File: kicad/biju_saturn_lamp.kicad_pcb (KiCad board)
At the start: 2 copper layers, 82.3 x 59.9 mm, 25 parts, among them J1 Barrel_Jack, J2 Conn_01x06, J3 Conn_01x02, J4 Conn_01x02, J5 Conn_01x02, SW1 SW_Push, U1 Pico, U2 74HC595, U3 PAM8302AAD

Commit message: update pcb
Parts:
- C4, C5: value 220uF -> 220nF
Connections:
- U2 pad 10: unconnected-(U2-~{SRCLR}-Pad10) -> VCC
- U2 pad 13: unconnected-(U2-~{OE}-Pad13) -> GND
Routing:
- net GND: track 45.4 -> 269.8 mm
- net VCC: track 153.5 -> 218.0 mm

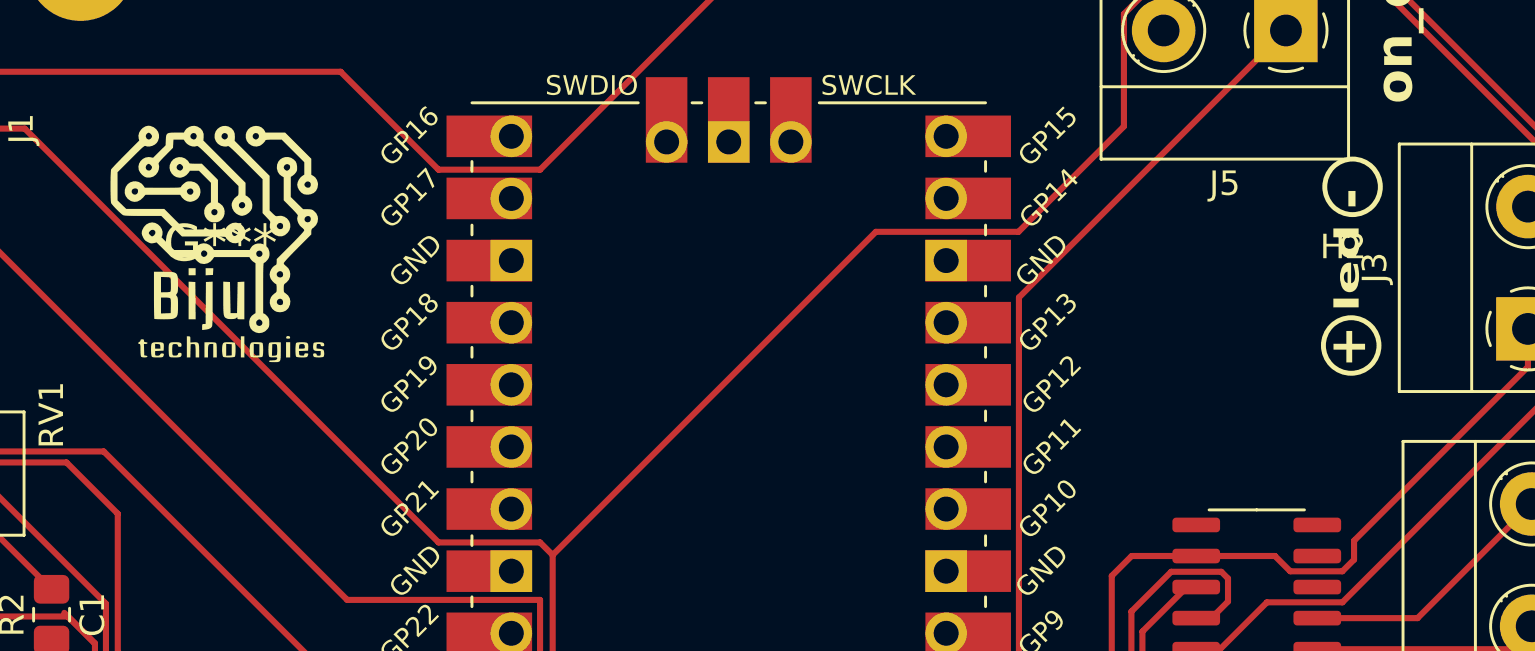
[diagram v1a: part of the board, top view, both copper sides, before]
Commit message: add logo to pcb
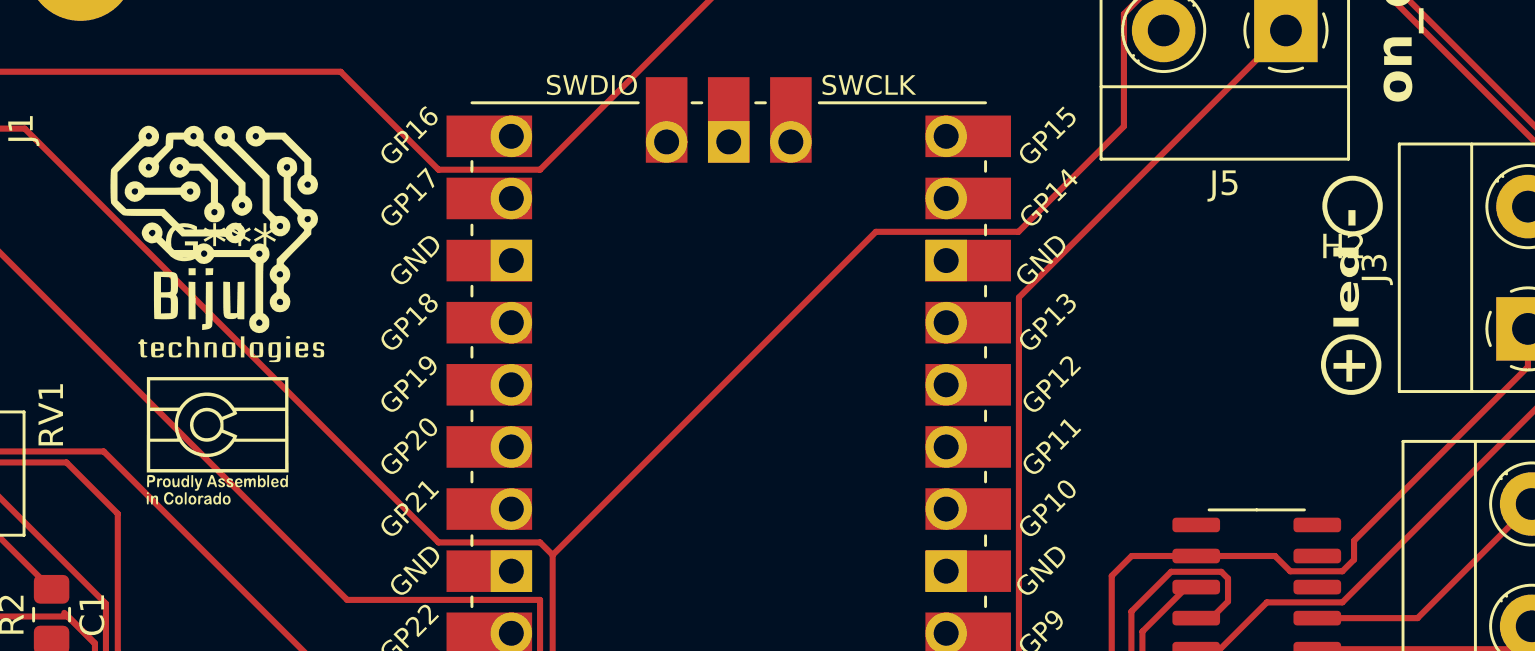
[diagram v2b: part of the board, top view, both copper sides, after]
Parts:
- added G***: LOGO, LOGO, F.Cu at (170.1, 113.5)

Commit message: update pcb
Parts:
- moved G*** 52.8 mm to (218.4, 125.7)
- moved G*** 52.8 mm to (211.6, 146.2)
- moved H3 9.14 mm to (180.3, 81.8)
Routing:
- net GND: track 269.8 -> 313.3 mm
- net VCC: track 218.0 -> 246.2 mm
- net GPIO8: track 53.5 -> 59.5 mm
- net 3v3_EN: track 119.0 -> 121.0 mm

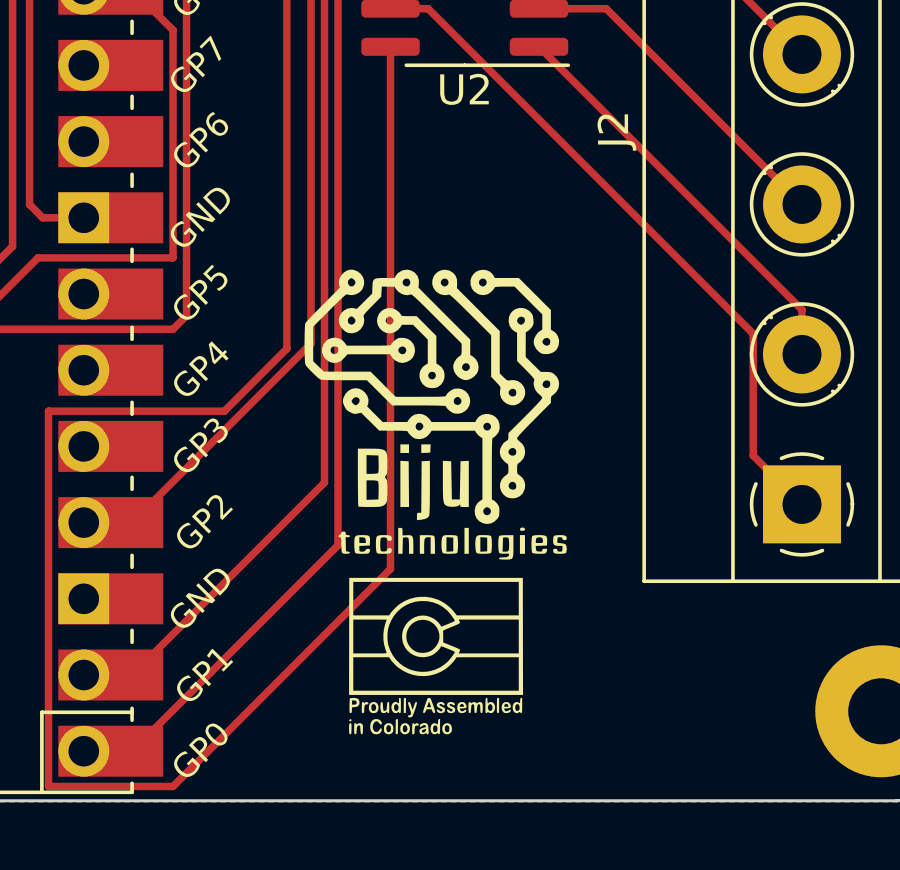
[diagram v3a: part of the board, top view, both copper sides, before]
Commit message: add logo to pcb
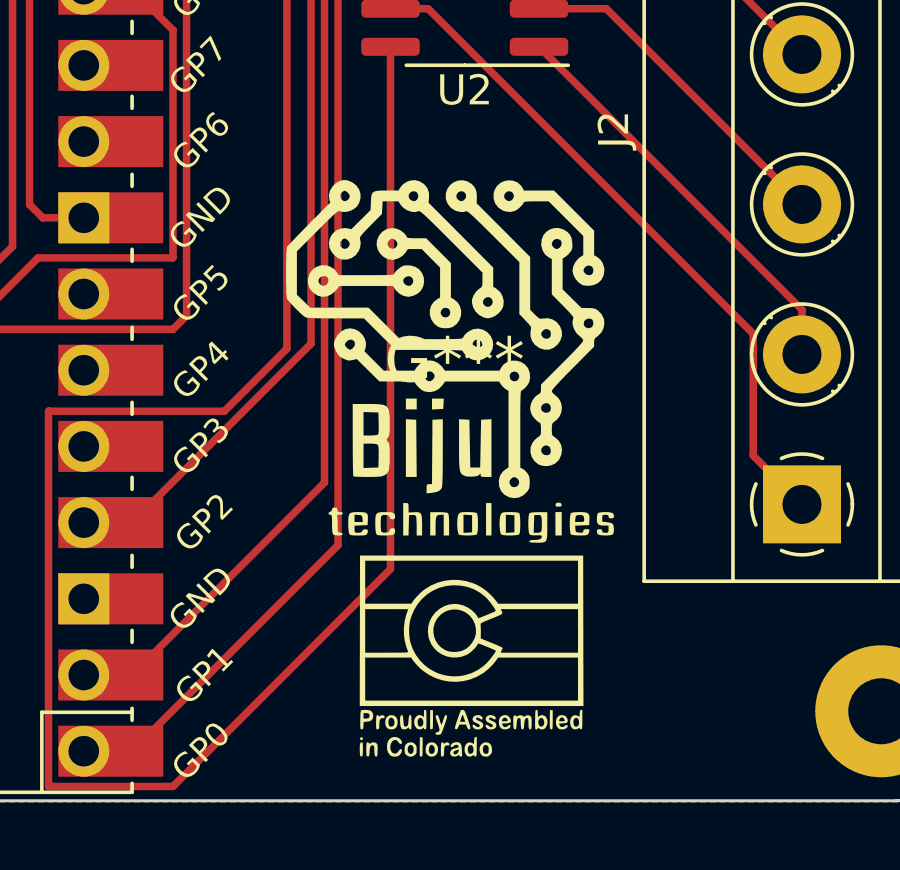
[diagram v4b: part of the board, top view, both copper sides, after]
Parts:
- removed the G*** at (211.6, 146.2)
- removed the G*** at (218.4, 125.7)
- added G***: LOGO, LOGO, F.Cu at (210.8, 149.7)
- added G***: LOGO, LOGO, F.Cu at (218.9, 124.0)

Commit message: update pcb
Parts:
- moved RV1 1.03 mm to (166.4, 99.1)
- moved R1 0.99 mm to (170.0, 112.3), turned to -90 degrees
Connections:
- U1 pad 18: unconnected-(U1-GND-Pad18) -> GND
- U1 pad 23: unconnected-(U1-GND-Pad23) -> GND
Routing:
- net GND: track 313.3 -> 229.3 mm
- net 3v3: track 70.5 -> 66.2 mm
- net Net-(C1-Pad2): track 2.54 -> 4.88 mm
- net Net-(C1-Pad1): track 7.53 -> 8.54 mm
- net Net-(U3-IN+): track 4.74 -> 3.86 mm
- net Net-(U3-~{SD}): track 26.5 -> 27.2 mm

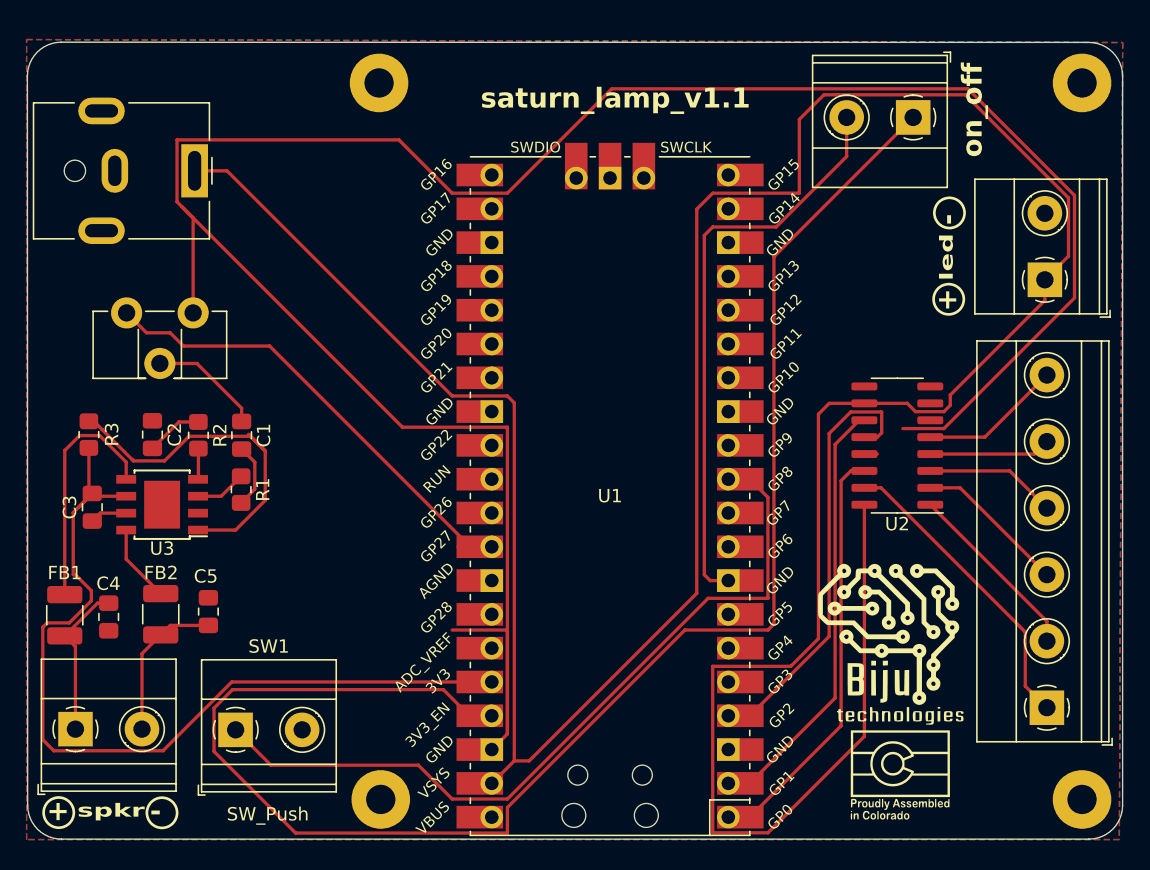
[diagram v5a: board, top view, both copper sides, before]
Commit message: fix on-off switch
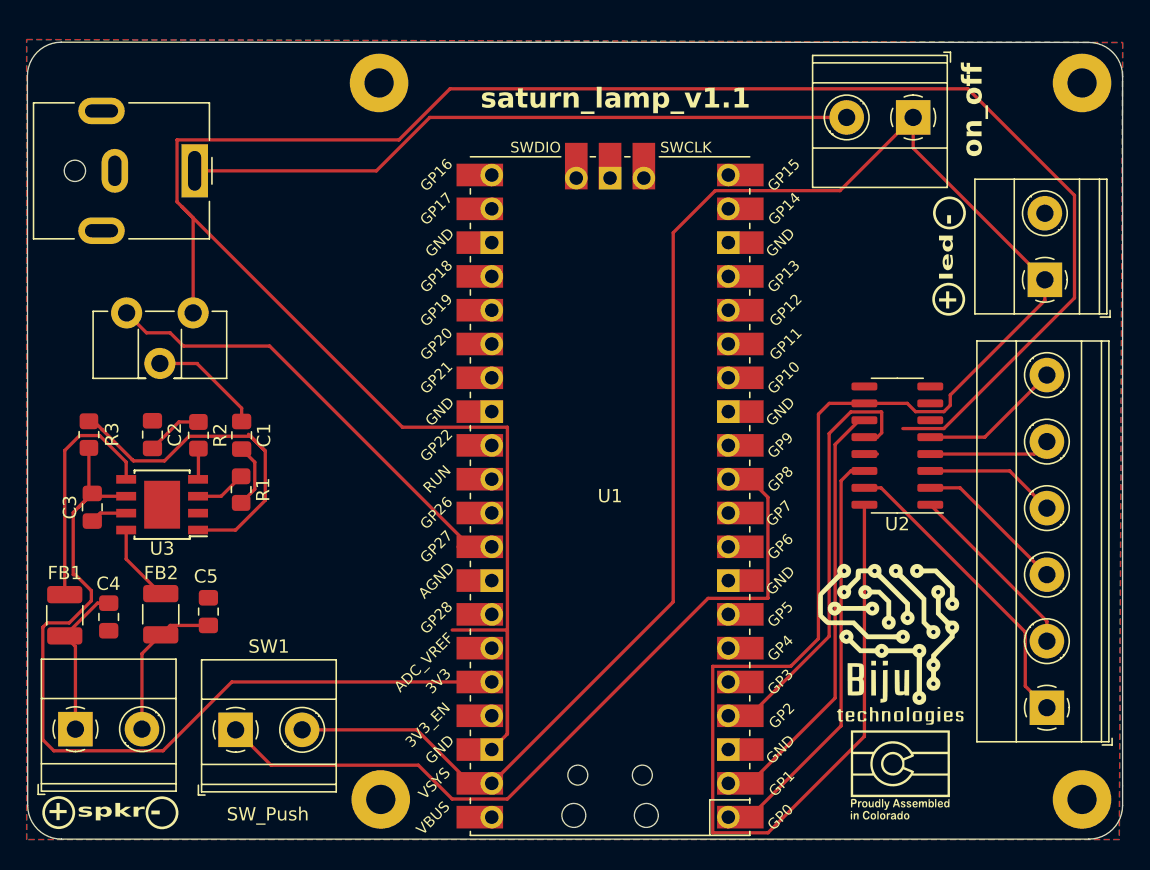
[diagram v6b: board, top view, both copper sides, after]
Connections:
- J1 pad 1: VCC -> Net-(J5-Pin_2)
- J5 pad 1: 3v3_EN -> VCC
- J5 pad 2: GND -> Net-(J5-Pin_2)
- SW1 pad 2: GND -> VCC
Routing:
- net 3v3_EN: track 121.0 -> 2.48 mm
- net VCC: track 246.7 -> 194.3 mm
- net Net-(J5-Pin_2): track 0.00 -> 50.7 mm
- net GND: track 229.3 -> 182.4 mm

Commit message: add base stl
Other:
- board text added: "JLCJLCJLCJLC"
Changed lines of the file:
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@@
     (fp_line (start 1.6 1.245) (end -1.6 1.245)
       (stroke (width 0.1) (type solid)) (layer "F.Fab"))
-    (pad "1" smd roundrect (at -1.55 0 270) (size 1.3 2.65) (layers "F.Cu" "F.Paste" "F.Mask") (roundrect_rratio 0.192308)
+    (pad "1" smd roundrect (at -1.55 0 270) (size 1.3 2.65) (layers "F.Cu" "F.Paste" "F.Mask") (roundrect_rratio 0.1923076923)
       (net 31 "Net-(U3-OUT+)") (pintype "passive"))
-    (pad "2" smd roundrect (at 1.55 0 270) (size 1.3 2.65) (layers "F.Cu" "F.Paste" "F.Mask") (roundrect_rratio 0.192308)
+    (pad "2" smd roundrect (at 1.55 0 270) (size 1.3 2.65) (layers "F.Cu" "F.Paste" "F.Mask") (roundrect_rratio 0.1923076923)
       (net 18 "Net-(J4-Pin_1)") (pintype "passive"))
     (model "${KICAD6_3DMODEL_DIR}/Resistor_SMD.3dshapes/R_1210_3225Metric.wrl"
@@
     (fp_line (start 1.6 1.245) (end -1.6 1.245)
       (stroke (width 0.1) (type solid)) (layer "F.Fab"))
-    (pad "1" smd roundrect (at -1.55 0 270) (size 1.3 2.65) (layers "F.Cu" "F.Paste" "F.Mask") (roundrect_rratio 0.192308)
+    (pad "1" smd roundrect (at -1.55 0 270) (size 1.3 2.65) (layers "F.Cu" "F.Paste" "F.Mask") (roundrect_rratio 0.1923076923)
       (net 32 "Net-(U3-OUT-)") (pintype "passive"))
-    (pad "2" smd roundrect (at 1.55 0 270) (size 1.3 2.65) (layers "F.Cu" "F.Paste" "F.Mask") (roundrect_rratio 0.192308)
+    (pad "2" smd roundrect (at 1.55 0 270) (size 1.3 2.65) (layers "F.Cu" "F.Paste" "F.Mask") (roundrect_rratio 0.1923076923)
       (net 25 "Net-(J4-Pin_2)") (pintype "passive"))
     (model "${KICAD6_3DMODEL_DIR}/Resistor_SMD.3dshapes/R_1210_3225Metric.wrl"
@@
     (fp_line (start 1 0.625) (end -1 0.625)
       (stroke (width 0.1) (type solid)) (layer "F.Fab"))
-    (pad "1" smd roundrect (at -1.0375 0 270) (size 1.175 1.45) (layers "F.Cu" "F.Paste" "F.Mask") (roundrect_rratio 0.212766)
+    (pad "1" smd roundrect (at -1.0375 0 270) (size 1.175 1.45) (layers "F.Cu" "F.Paste" "F.Mask") (roundrect_rratio 0.2127659574)
       (net 2 "GND") (pintype "passive"))
-    (pad "2" smd roundrect (at 1.0375 0 270) (size 1.175 1.45) (layers "F.Cu" "F.Paste" "F.Mask") (roundrect_rratio 0.212766)
+    (pad "2" smd roundrect (at 1.0375 0 270) (size 1.175 1.45) (layers "F.Cu" "F.Paste" "F.Mask") (roundrect_rratio 0.2127659574)
       (net 25 "Net-(J4-Pin_2)") (pintype "passive"))
     (model "${KICAD6_3DMODEL_DIR}/Capacitor_SMD.3dshapes/C_0805_2012Metric.wrl"
@@
     (fp_line (start 1 0.625) (end -1 0.625)
       (stroke (width 0.1) (type solid)) (layer "F.Fab"))
-    (pad "1" smd roundrect (at -1 0 90) (size 1.2 1.4) (layers "F.Cu" "F.Paste" "F.Mask") (roundrect_rratio 0.208333)
+    (pad "1" smd roundrect (at -1 0 90) (size 1.2 1.4) (layers "F.Cu" "F.Paste" "F.Mask") (roundrect_rratio 0.2083333333)
       (net 9 "3v3") (pintype "passive"))
-    (pad "2" smd roundrect (at 1 0 90) (size 1.2 1.4) (layers "F.Cu" "F.Paste" "F.Mask") (roundrect_rratio 0.208333)
+    (pad "2" smd roundrect (at 1 0 90) (size 1.2 1.4) (layers "F.Cu" "F.Paste" "F.Mask") (roundrect_rratio 0.2083333333)
       (net 28 "Net-(U3-~{SD})") (pintype "passive"))
     (model "${KICAD6_3DMODEL_DIR}/Resistor_SMD.3dshapes/R_0805_2012Metric.wrl"
@@
     (fp_line (start 1 0.625) (end -1 0.625)
       (stroke (width 0.1) (type solid)) (layer "F.Fab"))
-    (pad "1" smd roundrect (at -1 0 270) (size 1.2 1.4) (layers "F.Cu" "F.Paste" "F.Mask") (roundrect_rratio 0.208333)
+    (pad "1" smd roundrect (at -1 0 270) (size 1.2 1.4) (layers "F.Cu" "F.Paste" "F.Mask") (roundrect_rratio 0.2083333333)
       (net 26 "Net-(U3-IN+)") (pintype "passive"))
-    (pad "2" smd roundrect (at 1 0 270) (size 1.2 1.4) (layers "F.Cu" "F.Paste" "F.Mask") (roundrect_rratio 0.208333)
+    (pad "2" smd roundrect (at 1 0 270) (size 1.2 1.4) (layers "F.Cu" "F.Paste" "F.Mask") (roundrect_rratio 0.2083333333)
       (net 8 "Net-(C1-Pad2)") (pintype "passive"))
     (model "${KICAD6_3DMODEL_DIR}/Resistor_SMD.3dshapes/R_0805_2012Metric.wrl"
@@
     (fp_line (start 1 0.625) (end -1 0.625)
       (stroke (width 0.1) (type solid)) (layer "F.Fab"))
-    (pad "1" smd roundrect (at -1.0375 0 270) (size 1.175 1.45) (layers "F.Cu" "F.Paste" "F.Mask") (roundrect_rratio 0.212766)
+    (pad "1" smd roundrect (at -1.0375 0 270) (size 1.175 1.45) (layers "F.Cu" "F.Paste" "F.Mask") (roundrect_rratio 0.2127659574)
       (net 7 "Net-(C1-Pad1)") (pintype "passive"))
-    (pad "2" smd roundrect (at 1.0375 0 270) (size 1.175 1.45) (layers "F.Cu" "F.Paste" "F.Mask") (roundrect_rratio 0.212766)
+    (pad "2" smd roundrect (at 1.0375 0 270) (size 1.175 1.45) (layers "F.Cu" "F.Paste" "F.Mask") (roundrect_rratio 0.2127659574)
       (net 8 "Net-(C1-Pad2)") (pintype "passive"))
     (model "${KICAD6_3DMODEL_DIR}/Capacitor_SMD.3dshapes/C_0805_2012Metric.wrl"
@@
     (fp_line (start 1 0.625) (end -1 0.625)
       (stroke (width 0.1) (type solid)) (layer "F.Fab"))
-    (pad "1" smd roundrect (at -1.0375 0 90) (size 1.175 1.45) (layers "F.Cu" "F.Paste" "F.Mask") (roundrect_rratio 0.212766)
+    (pad "1" smd roundrect (at -1.0375 0 90) (size 1.175 1.45) (layers "F.Cu" "F.Paste" "F.Mask") (roundrect_rratio 0.2127659574)
       (net 2 "GND") (pintype "passive"))
-    (pad "2" smd roundrect (at 1.0375 0 90) (size 1.175 1.45) (layers "F.Cu" "F.Paste" "F.Mask") (roundrect_rratio 0.212766)
+    (pad "2" smd roundrect (at 1.0375 0 90) (size 1.175 1.45) (layers "F.Cu" "F.Paste" "F.Mask") (roundrect_rratio 0.2127659574)
       (net 9 "3v3") (pintype "passive"))
     (model "${KICAD6_3DMODEL_DIR}/Capacitor_SMD.3dshapes/C_0805_2012Metric.wrl"
@@
     (fp_line (start 1 0.625) (end -1 0.625)
       (stroke (width 0.1) (type solid)) (layer "F.Fab"))
-    (pad "1" smd roundrect (at -1.0375 0 90) (size 1.175 1.45) (layers "F.Cu" "F.Paste" "F.Mask") (roundrect_rratio 0.212766)
+    (pad "1" smd roundrect (at -1.0375 0 90) (size 1.175 1.45) (layers "F.Cu" "F.Paste" "F.Mask") (roundrect_rratio 0.2127659574)
       (net 2 "GND") (pintype "passive"))
-    (pad "2" smd roundrect (at 1.0375 0 90) (size 1.175 1.45) (layers "F.Cu" "F.Paste" "F.Mask") (roundrect_rratio 0.212766)
+    (pad "2" smd roundrect (at 1.0375 0 90) (size 1.175 1.45) (layers "F.Cu" "F.Paste" "F.Mask") (roundrect_rratio 0.2127659574)
       (net 18 "Net-(J4-Pin_1)") (pintype "passive"))
     (model "${KICAD6_3DMODEL_DIR}/Capacitor_SMD.3dshapes/C_0805_2012Metric.wrl"
@@
     (fp_line (start 1 0.625) (end -1 0.625)
       (stroke (width 0.1) (type solid)) (layer "F.Fab"))
-    (pad "1" smd roundrect (at -1 0 90) (size 1.2 1.4) (layers "F.Cu" "F.Paste" "F.Mask") (roundrect_rratio 0.208333)
+    (pad "1" smd roundrect (at -1 0 90) (size 1.2 1.4) (layers "F.Cu" "F.Paste" "F.Mask") (roundrect_rratio 0.2083333333)
       (net 27 "Net-(U3-IN-)") (pintype "passive"))
-    (pad "2" smd roundrect (at 1 0 90) (size 1.2 1.4) (layers "F.Cu" "F.Paste" "F.Mask") (roundrect_rratio 0.208333)
+    (pad "2" smd roundrect (at 1 0 90) (size 1.2 1.4) (layers "F.Cu" "F.Paste" "F.Mask") (roundrect_rratio 0.2083333333)
       (net 17 "Net-(C2-Pad2)") (pintype "passive"))
     (model "${KICAD6_3DMODEL_DIR}/Resistor_SMD.3dshapes/R_0805_2012Metric.wrl"
@@
     (fp_line (start 1 0.625) (end -1 0.625)
       (stroke (width 0.1) (type solid)) (layer "F.Fab"))
-    (pad "1" smd roundrect (at -1.0375 0 270) (size 1.175 1.45) (layers "F.Cu" "F.Paste" "F.Mask") (roundrect_rratio 0.212766)
+    (pad "1" smd roundrect (at -1.0375 0 270) (size 1.175 1.45) (layers "F.Cu" "F.Paste" "F.Mask") (roundrect_rratio 0.2127659574)
       (net 2 "GND") (pintype "passive"))
-    (pad "2" smd roundrect (at 1.0375 0 270) (size 1.175 1.45) (layers "F.Cu" "F.Paste" "F.Mask") (roundrect_rratio 0.212766)
+    (pad "2" smd roundrect (at 1.0375 0 270) (size 1.175 1.45) (layers "F.Cu" "F.Paste" "F.Mask") (roundrect_rratio 0.2127659574)
       (net 17 "Net-(C2-Pad2)") (pintype "passive"))
     (model "${KICAD6_3DMODEL_DIR}/Capacitor_SMD.3dshapes/C_0805_2012Metric.wrl"
@@
   (gr_arc (start 156.471051 138.618949) (mid 154.675 137.875) (end 153.931051 136.078949)
     (stroke (width 0.1) (type default)) (layer "Edge.Cuts"))
+  (gr_text "JLCJLCJLCJLC" (at 156.464 81.788) (layer "B.SilkS")
+    (effects (font (size 1.5 1.5) (thickness 0.3) bold) (justify left bottom))
+  )
   (gr_text "led" (at 223.576 96.658077 90) (layer "F.SilkS")
     (effects (font (size 0.992 1.5) (thickness 0.248) bold) (justify left bottom))
